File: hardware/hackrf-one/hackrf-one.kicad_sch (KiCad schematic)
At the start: 0 parts

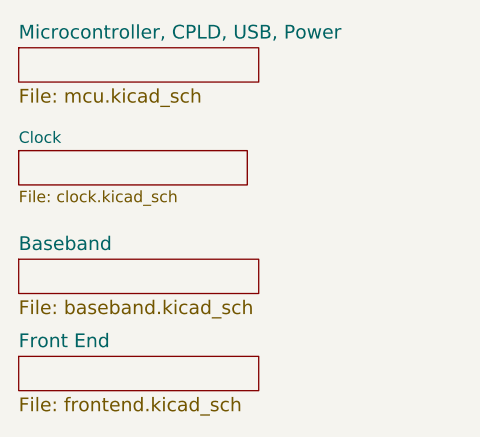
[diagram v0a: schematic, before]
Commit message: HackRF One: revert hardware design to 8727449
This commit is between r8 and r9 and will be used as the basis for r10.
It includes some of the changes in r9 but predates the major changes to
the clock generator and IF transceiver ICs.
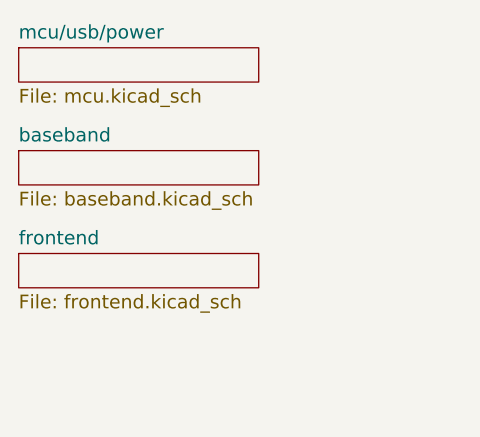
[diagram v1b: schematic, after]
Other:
- sheet Baseband renamed baseband
- sheet Front End renamed frontend
- sheet Microcontroller, CPLD, USB, Power renamed mcu/usb/power
- removed sheet Clock

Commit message: HackRF One: update version to 8+
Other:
- company: Copyright 2012-2022 Great Scott Gadgets -> ${COPYRIGHT}
- title: HackRF One -> ${TITLE}
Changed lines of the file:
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@@
   (paper "User" 431.8 279.4)
   (title_block
-    (title "HackRF One")
-    (date "2022-08-28")
-    (rev "r9")
-    (company "Copyright 2012-2022 Great Scott Gadgets")
-    (comment 1 "Michael Ossmann")
-    (comment 2 "Licensed under the CERN-OHL-P v2")
+    (title "${TITLE}")
+    (date "${DATE}")
+    (rev "${VERSION}")
+    (company "${COPYRIGHT}")
+    (comment 1 "${LICENSE}")
   )
   (sheet (at 64.77 60.96) (size 26.67 3.81) (fields_autoplaced)
